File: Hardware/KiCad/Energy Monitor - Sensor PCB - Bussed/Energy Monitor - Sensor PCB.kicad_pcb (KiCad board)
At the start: 4 copper layers, 80 x 100 mm, 127 parts, among them IC1 ATM90E36, IC2 ATM90E36, J1 Conn_02x05_Odd_Even, J2 Conn_02x17_Odd_Even, J3 Conn_02x14_Odd_Even, Q1 RUM002N05T2LCT-ND, Q2 RUM002N05T2LCT-ND, Q3 RUM002N05T2LCT-ND, Y1 16.384MHz, Y2 16.384MHz

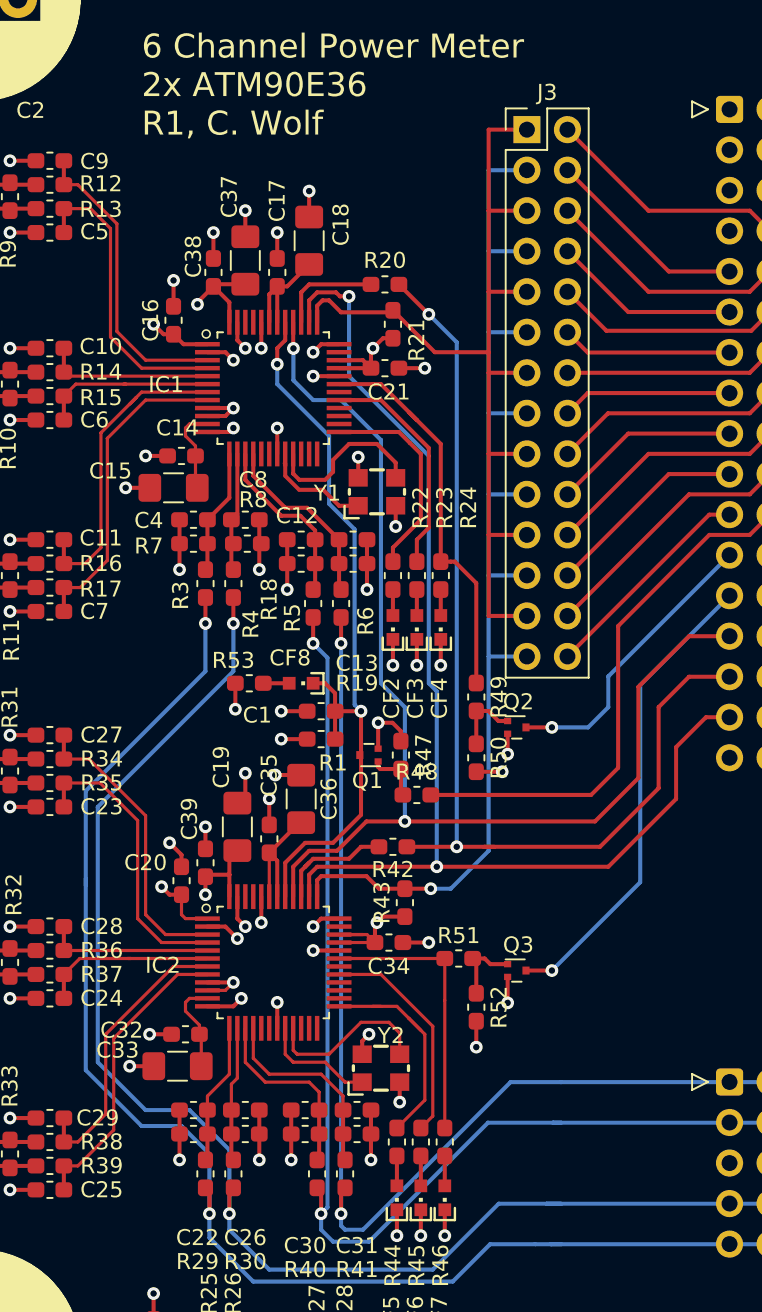
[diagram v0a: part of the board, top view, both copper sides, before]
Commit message: Common-bus variant of the power monitor.
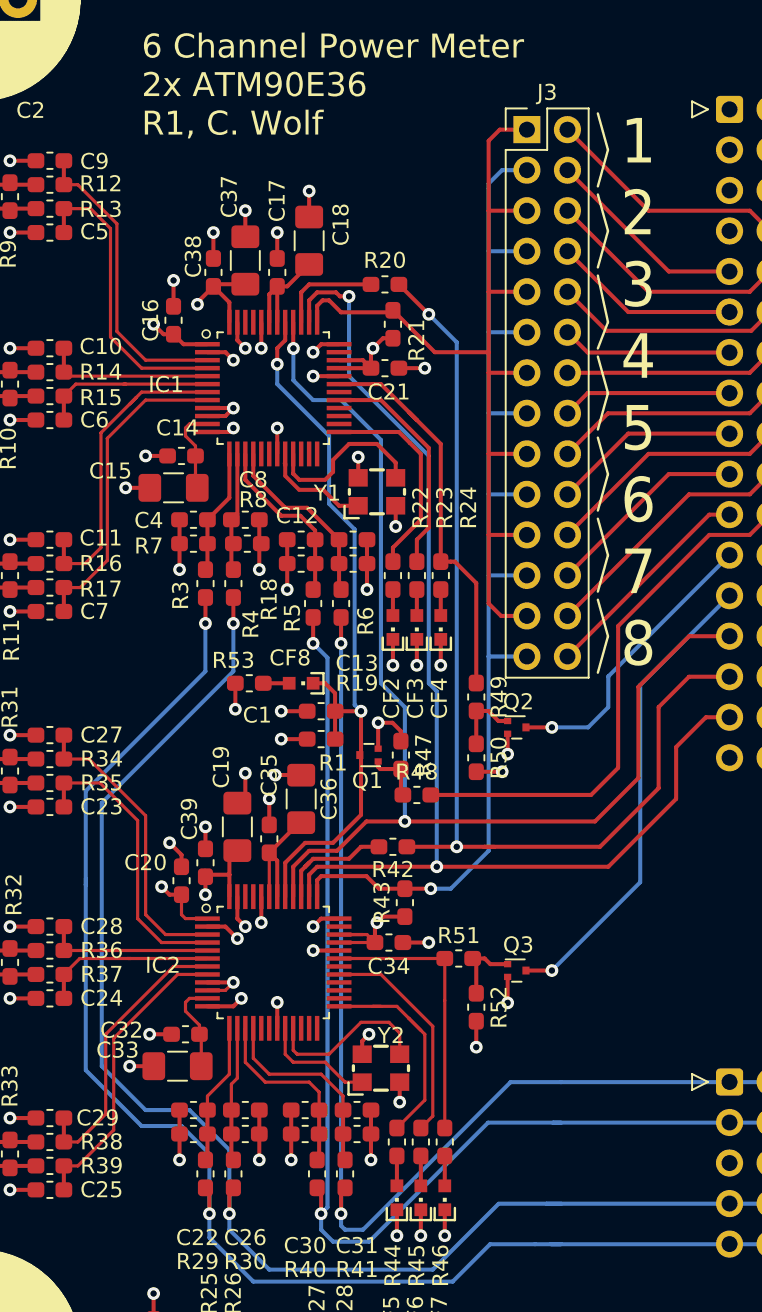
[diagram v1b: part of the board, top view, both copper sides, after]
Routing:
- net /meter_1/~CS: track 60.7 -> 59.8 mm
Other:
- board text added: "1 2 3 4 5 6 7 8"
